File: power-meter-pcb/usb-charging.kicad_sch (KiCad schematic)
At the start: 4 parts, among them J1 USB4105-GF-A, U1 TPD3E001DRLR

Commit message: Assigning footprints, extremely rough idea of size
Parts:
- J1: footprint USB4105-GF-A:GCT_USB4105-GF-A -> USB4105:GCT_USB4105-GF-A
- R1, R4: footprint (none) -> Resistor_SMD:R_0603_1608Metric_Pad0.98x0.95mm_HandSolder
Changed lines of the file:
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@@
 			)
 		)
-		(property "Footprint" ""
+		(property "Footprint" "Resistor_SMD:R_0603_1608Metric_Pad0.98x0.95mm_HandSolder"
 			(at 135.382 74.93 90)
 			(effects
@@
 			)
 		)
-		(property "Footprint" ""
+		(property "Footprint" "Resistor_SMD:R_0603_1608Metric_Pad0.98x0.95mm_HandSolder"
 			(at 61.722 72.39 90)
 			(effects
@@
 			)
 		)
-		(property "Footprint" "USB4105-GF-A:GCT_USB4105-GF-A"
+		(property "Footprint" "USB4105:GCT_USB4105-GF-A"
 			(at 101.6 71.12 0)
 			(effects

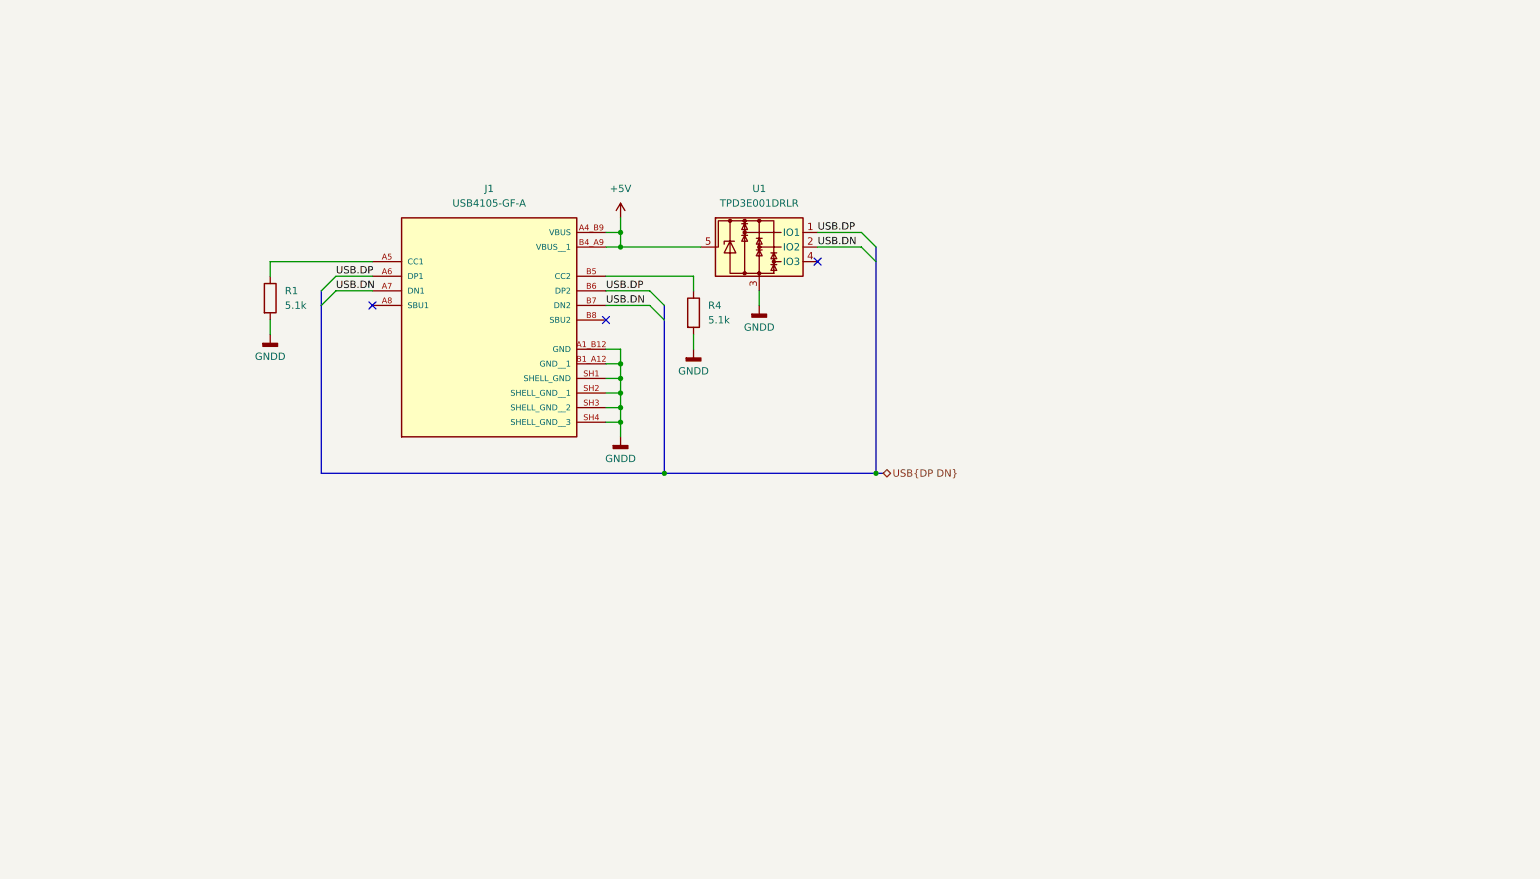
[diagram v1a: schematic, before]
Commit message: Added power supply to PCB
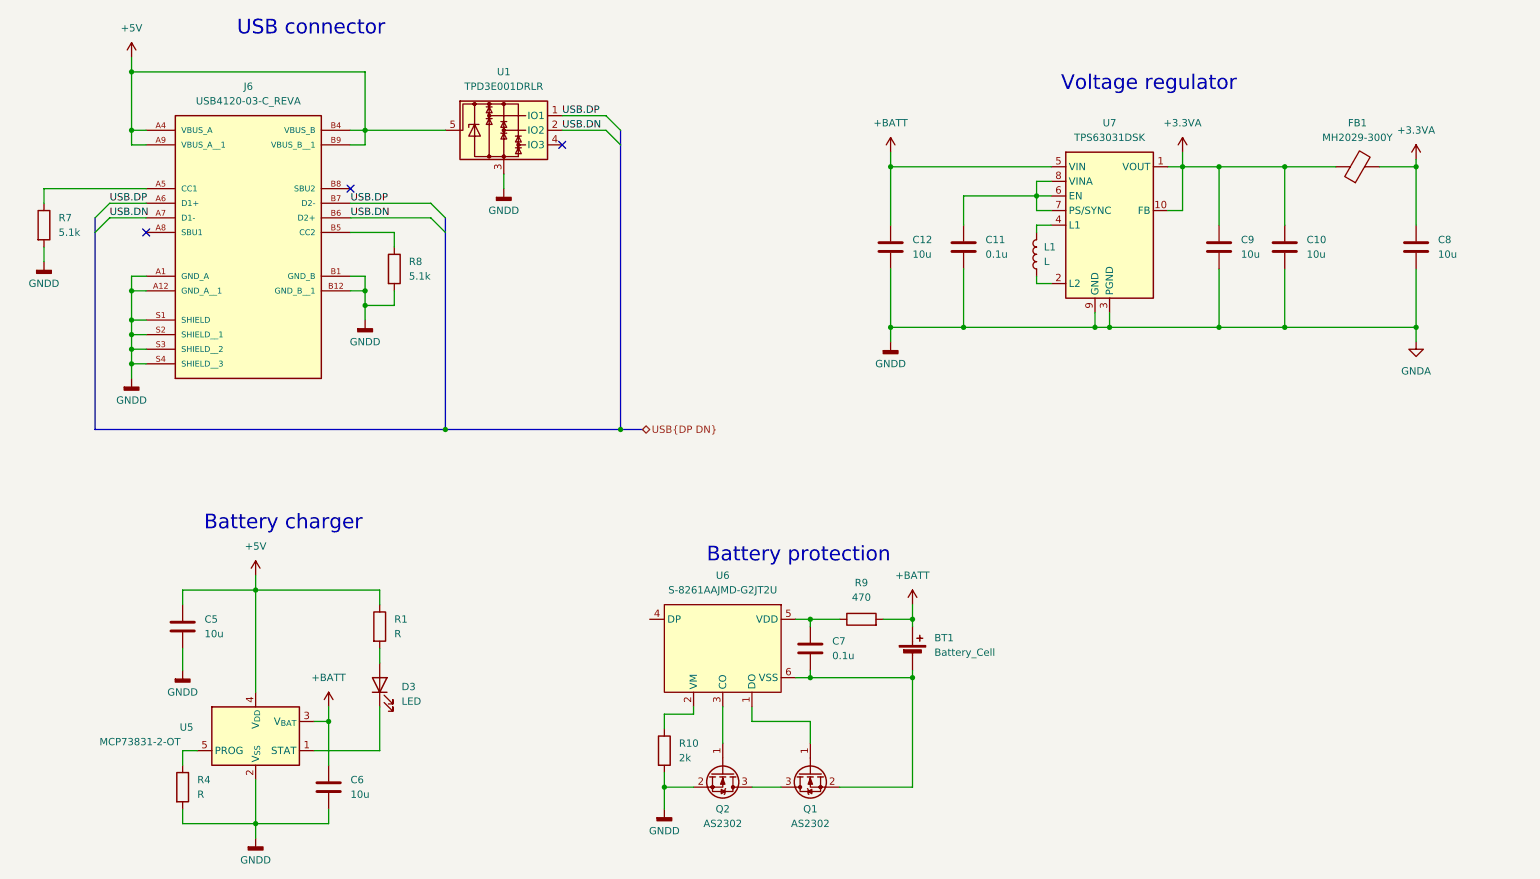
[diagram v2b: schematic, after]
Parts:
- removed J1: USB4105-GF-A, USB4105:GCT_USB4105-GF-A, symbol USB4105:USB4105-GF-A
- added BT1: Battery_Cell, symbol Device:Battery_Cell
- added C10, C12, C5, C6, C8, C9: 10u, symbol Device:C
- added C11, C7: 0.1u, symbol Device:C
- added D3: LED, symbol Device:LED
- added FB1: MH2029-300Y, symbol Device:FerriteBead
- added J6: USB4120-03-C_REVA, USB4120:GCT_USB4120-03-C_REVA, symbol USB4120-03-C_REVA:USB4120-03-C_REVA
- added L1: L, symbol Device:L
- added Q1, Q2: AS2302, symbol Device:Q_NMOS_GSD
- added R10: 2k, symbol Device:R
- added R7, R8: 5.1k, Resistor_SMD:R_0603_1608Metric_Pad0.98x0.95mm_HandSolder, symbol Device:R
- added R9: 470, symbol Device:R
- added U5: MCP73831-2-OT, Package_TO_SOT_SMD:SOT-23-5, symbol Battery_Management:MCP73831-2-OT
- added U6: S-8261AAJMD-G2JT2U, Package_TO_SOT_SMD:SOT-23-6, symbol Custom:S-8261_Battery_protection_IC
- added U7: TPS63031DSK, Package_SON:WSON-10-1EP_2.5x2.5mm_P0.5mm_EP1.2x2mm, symbol Regulator_Switching:TPS63031DSK
- R1, R4: value 5.1k -> R; footprint Resistor_SMD:R_0603_1608Metric_Pad0.98x0.95mm_HandSolder -> (none)
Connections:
- net +5V: now also R1.1, C5.1, J6.A4 (VBUS_A), J6.A9 (VBUS_A__1), J6.B4 (VBUS_B), J6.B9 (VBUS_B__1), U5.4 (V_{DD})
- net USB.DN: now also J6.A7 (D1-), J6.B6 (D2+)
- net USB.DP: now also J6.A6 (D1+), J6.B7 (D2-)
- net at R4.1: now also U5.5 (PROG)
- net GNDD renamed GNDA
- net GNDA: now also C10.2, C11.2, C12.2, C5.2, C6.2, C8.2, C9.2, J6.A1 (GND_A), J6.A12 (GND_A__1), J6.B1 (GND_B), J6.B12 (GND_B__1), J6.S1 (SHIELD), J6.S2 (SHIELD__1), J6.S3 (SHIELD__2), J6.S4 (SHIELD__3), Q2.2 (S), R10.2, R7.2, R8.2, U5.2 (V_{SS}), U7.11 (PGND), U7.3 (PGND), U7.9 (GND); no longer R1.2
- new net: J6.B5 (CC2), R8.1
- new net: D3.2 (A), R1.2
- new net: J6.A5 (CC1), R7.1
- new net: R10.1, U6.2 (VM)
- new net: L1.1, U7.2 (L2)
- new net: L1.2, U7.4 (L1)
- new net: C11.1, U7.6 (EN), U7.7 (PS/SYNC), U7.8 (VINA)
- new net: D3.1 (K), U5.1 (STAT)
- new net: C7.1, R9.1, U6.5 (VDD)
- new net: Q1.1 (G), U6.1 (DO)
- new net: BT1.2 (-), C7.2, Q1.2 (S), U6.6 (VSS)
- new net: Q1.3 (D), Q2.3 (D)
- new net: Q2.1 (G), U6.3 (CO)
- new net +3.3VA: C10.1, C8.1, C9.1, FB1.1, FB1.2, U7.1 (VOUT), U7.10 (FB)
- new net +BATT: BT1.1 (+), C12.1, C6.1, R9.2, U5.3 (V_{BAT}), U7.5 (VIN)
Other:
- note added: "Battery charger"
- note added: "Battery protection"
- note added: "USB connector"
- note added: "Voltage regulator"
- moved on the sheet: U1

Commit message: Started PCB layout
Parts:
- added C15: 0.1u, Capacitor_SMD:C_0603_1608Metric_Pad1.08x0.95mm_HandSolder, symbol Device:C
- added R11, R12: 1M, Resistor_SMD:R_0603_1608Metric_Pad0.98x0.95mm_HandSolder, symbol Device:R
- BT1: footprint (none) -> Connector_JST:JST_EH_B2B-EH-A_1x02_P2.50mm_Vertical
- C10: renamed from C8; footprint (none) -> Capacitor_SMD:C_0603_1608Metric_Pad1.08x0.95mm_HandSolder
- C3: renamed from C5; footprint (none) -> Capacitor_SMD:C_0603_1608Metric_Pad1.08x0.95mm_HandSolder
- C4: renamed from C6; footprint (none) -> Capacitor_SMD:C_0603_1608Metric_Pad1.08x0.95mm_HandSolder
- C5: renamed from C7; footprint (none) -> Capacitor_SMD:C_0603_1608Metric_Pad1.08x0.95mm_HandSolder
- C6: renamed from C12; footprint (none) -> Capacitor_SMD:C_0603_1608Metric_Pad1.08x0.95mm_HandSolder
- C7: renamed from C11; footprint (none) -> Capacitor_SMD:C_0603_1608Metric_Pad1.08x0.95mm_HandSolder
- C8: renamed from C9; footprint (none) -> Capacitor_SMD:C_0603_1608Metric_Pad1.08x0.95mm_HandSolder
- C9: renamed from C10; footprint (none) -> Capacitor_SMD:C_0603_1608Metric_Pad1.08x0.95mm_HandSolder
- D3: footprint (none) -> LED_SMD:LED_0603_1608Metric_Pad1.05x0.95mm_HandSolder
- FB1: footprint (none) -> Inductor_SMD:L_0805_2012Metric
- L1: value L -> 4.7uH; footprint (none) -> Inductor_SMD:L_Murata_DFE201610P
- Q1: renamed from Q2; footprint (none) -> Package_TO_SOT_SMD:TSOT-23
- Q2: renamed from Q1; footprint (none) -> Package_TO_SOT_SMD:TSOT-23
- R10: renamed from R9; footprint (none) -> Resistor_SMD:R_0603_1608Metric_Pad0.98x0.95mm_HandSolder
- R6: renamed from R4; value R -> 2.2k; footprint (none) -> Resistor_SMD:R_0603_1608Metric_Pad0.98x0.95mm_HandSolder
- R7: renamed from R1; value R -> 470; footprint (none) -> Resistor_SMD:R_0603_1608Metric_Pad0.98x0.95mm_HandSolder
- R9: renamed from R10; footprint (none) -> Resistor_SMD:R_0603_1608Metric_Pad0.98x0.95mm_HandSolder
- renumbered J6 to J3, R7 to R5, U5 to U3, U1 to U4, U6 to U5, U7 to U6
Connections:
- net +3.3VA: no longer C8.1, C9.1, FB1.1, U6.1 (VOUT), U6.10 (FB)
- net +BATT: now also R12.1
- net GNDA: no longer C3.2, C4.2, C6.2, C7.2, C8.2, C9.2, J3.A1 (GND_A), J3.A12 (GND_A__1), J3.B1 (GND_B), J3.B12 (GND_B__1), J3.S1 (SHIELD), J3.S2 (SHIELD__1), J3.S3 (SHIELD__2), J3.S4 (SHIELD__3), Q1.2 (S), R5.2, R6.2, R8.2, R9.2, U3.2 (V_{SS}), U4.3, U6.11 (PGND), U6.3 (PGND), U6.9 (GND)
- net at C7.1, U6.6 (EN), U6.8 (VINA): no longer U6.7 (PS/SYNC)
- new net +3.3V: C8.1, C9.1, FB1.1, U6.1 (VOUT), U6.10 (FB)
- new net Battery voltage: C15.1, R11.1, R12.2
- new net GNDD: C15.2, C3.2, C4.2, C6.2, C7.2, C8.2, C9.2, J3.A1 (GND_A), J3.A12 (GND_A__1), J3.B1 (GND_B), J3.B12 (GND_B__1), J3.S1 (SHIELD), J3.S2 (SHIELD__1), J3.S3 (SHIELD__2), J3.S4 (SHIELD__3), Q1.2 (S), R11.2, R5.2, R6.2, R8.2, R9.2, U3.2 (V_{SS}), U4.3, U6.11 (PGND), U6.3 (PGND), U6.9 (GND)
- new net Power save: U6.7 (PS/SYNC)
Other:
- note added: "Battery voltage measurement"
- moved on the sheet: BT1, C6, C7, FB1, L1

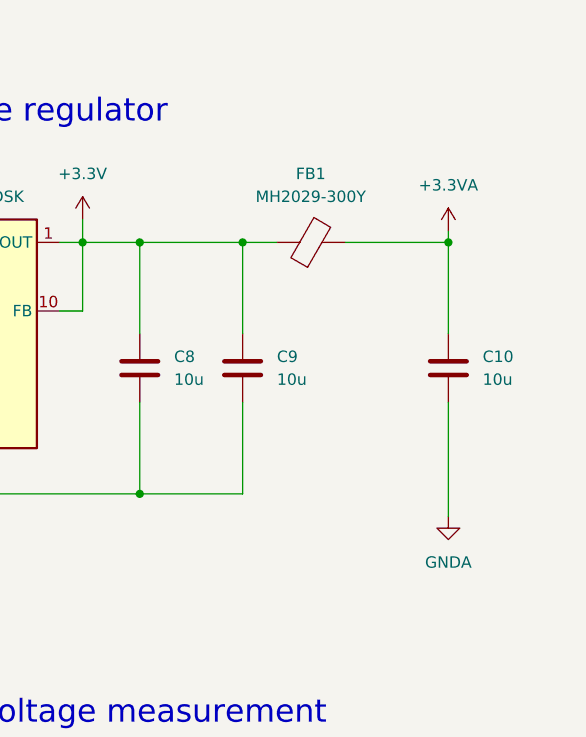
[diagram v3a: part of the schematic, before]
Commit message: Adding filtering and pullup resistors, board layout
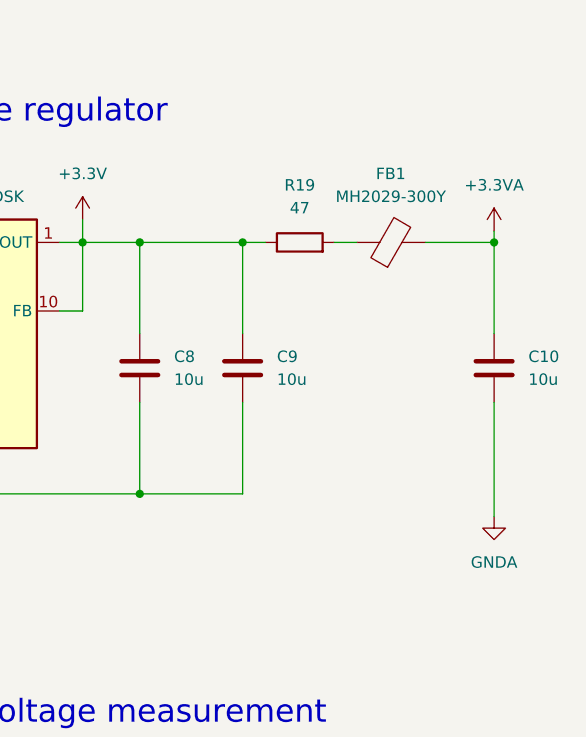
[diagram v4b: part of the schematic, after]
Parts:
- added R19: 47, Resistor_SMD:R_0603_1608Metric_Pad0.98x0.95mm_HandSolder, symbol Device:R
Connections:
- net +3.3V: now also R19.1; no longer FB1.1
- new net: FB1.1, R19.2
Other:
- moved on the sheet: C10, FB1
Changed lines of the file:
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@@
 	)
 	(junction
-		(at 262.89 49.53)
+		(at 267.97 49.53)
 		(diameter 0)
 		(color 0 0 0 0)
@@
 	(wire
 		(pts
-			(xy 262.89 67.31) (xy 262.89 80.01)
+			(xy 267.97 67.31) (xy 267.97 80.01)
 		)
 		(stroke
@@
 	(wire
 		(pts
-			(xy 251.46 49.53) (xy 262.89 49.53)
-		)
-		(stroke
-			(width 0)
-			(type default)
-		)
-	)
-	(wire
-		(pts
 			(xy 80.01 43.18) (xy 80.01 33.02)
 		)
@@
 	(wire
 		(pts
-			(xy 262.89 48.26) (xy 262.89 49.53)
+			(xy 267.97 48.26) (xy 267.97 49.53)
 		)
 		(stroke
@@
 	(wire
 		(pts
-			(xy 240.03 49.53) (xy 243.84 49.53)
+			(xy 240.03 49.53) (xy 242.57 49.53)
 		)
 		(stroke
@@
 	(wire
 		(pts
+			(xy 260.35 49.53) (xy 267.97 49.53)
+		)
+		(stroke
+			(width 0)
+			(type default)
+		)
+	)
+	(wire
+		(pts
 			(xy 219.71 137.16) (xy 219.71 139.7)
 		)
@@
 	(wire
 		(pts
-			(xy 262.89 49.53) (xy 262.89 59.69)
+			(xy 267.97 49.53) (xy 267.97 59.69)
 		)
 		(stroke
@@
 		(pts
 			(xy 157.48 128.27) (xy 162.56 128.27)
+		)
+		(stroke
+			(width 0)
+			(type default)
+		)
+	)
+	(wire
+		(pts
+			(xy 250.19 49.53) (xy 252.73 49.53)
 		)
 		(stroke
@@
 	(symbol
 		(lib_id "Device:R")
+		(at 246.38 49.53 90)
+		(unit 1)
+		(exclude_from_sim no)
+		(in_bom yes)
+		(on_board yes)
+		(dnp no)
+		(fields_autoplaced yes)
+		(property "Reference" "R19"
+			(at 246.38 43.18 90)
+			(effects
+				(font
+					(size 1.27 1.27)
+				)
+			)
+		)
+		(property "Value" "47"
+			(at 246.38 45.72 90)
+			(effects
+				(font
+					(size 1.27 1.27)
+				)
+			)
+		)
+		(property "Footprint" "Resistor_SMD:R_0603_1608Metric_Pad0.98x0.95mm_HandSolder"
+			(at 246.38 51.308 90)
+			(effects
+				(font
+					(size 1.27 1.27)
+				)
+				(hide yes)
+			)
+		)
+		(property "Datasheet" "~"
+			(at 246.38 49.53 0)
+			(effects
+				(font
+					(size 1.27 1.27)
+				)
+				(hide yes)
+			)
+		)
+		(property "Description" "Resistor"
+			(at 246.38 49.53 0)
+			(effects
+				(font
+					(size 1.27 1.27)
+				)
+				(hide yes)
+			)
+		)
+		(pin "2"
+		)
+		(pin "1"
+		)
+		(instances
+			(project "power-meter-pcb"
+				(path "/73d1dc3f-3725-4767-8c11-2d32e15ee0d6/4fb726d4-a68e-4ad8-a718-58b82440e761"
+					(reference "R19")
+					(unit 1)
+				)
+			)
+		)
+	)
+	(symbol
+		(lib_id "Device:R")
 		(at 219.71 118.11 0)
 		(unit 1)
@@
 	(symbol
 		(lib_id "power:+3.3VA")
-		(at 262.89 48.26 0)
+		(at 267.97 48.26 0)
 		(unit 1)
 		(exclude_from_sim no)
@@
 		(fields_autoplaced yes)
 		(property "Reference" "#PWR030"
-			(at 262.89 52.07 0)
+			(at 267.97 52.07 0)
 			(effects
 				(font
@@
 		)
 		(property "Value" "+3.3VA"
-			(at 262.89 43.18 0)
+			(at 267.97 43.18 0)
 			(effects
 				(font
@@
 		)
 		(property "Footprint" ""
-			(at 262.89 48.26 0)
+			(at 267.97 48.26 0)
 			(effects
 				(font
@@
 		)
 		(property "Datasheet" ""
-			(at 262.89 48.26 0)
+			(at 267.97 48.26 0)
 			(effects
 				(font
@@
 		)
 		(property "Description" "Power symbol creates a global label with name \"+3.3VA\""
-			(at 262.89 48.26 0)
+			(at 267.97 48.26 0)
 			(effects
 				(font
@@
 	(symbol
 		(lib_id "Device:FerriteBead")
-		(at 247.65 49.53 90)
+		(at 256.54 49.53 90)
 		(unit 1)
 		(exclude_from_sim no)
@@
 		(fields_autoplaced yes)
 		(property "Reference" "FB1"
-			(at 247.5992 41.91 90)
+			(at 256.4892 41.91 90)
 			(effects
 				(font
@@
 		)
 		(property "Value" "MH2029-300Y"
-			(at 247.5992 44.45 90)
+			(at 256.4892 44.45 90)
 			(effects
 				(font
@@
 		)
 		(property "Footprint" "Inductor_SMD:L_0805_2012Metric"
-			(at 247.65 51.308 90)
+			(at 256.54 51.308 90)
 			(effects
 				(font
@@
 		)
 		(property "Datasheet" "~"
-			(at 247.65 49.53 0)
+			(at 256.54 49.53 0)
 			(effects
 				(font
@@
 		)
 		(property "Description" "Ferrite bead"
-			(at 247.65 49.53 0)
+			(at 256.54 49.53 0)
 			(effects
 				(font
@@
 	(symbol
 		(lib_id "Device:C")
-		(at 262.89 63.5 0)
+		(at 267.97 63.5 0)
 		(unit 1)
 		(exclude_from_sim no)
@@
 		(fields_autoplaced yes)
 		(property "Reference" "C10"
-			(at 266.7 62.2299 0)
+			(at 271.78 62.2299 0)
 			(effects
 				(font
@@
 		)
 		(property "Value" "10u"
-			(at 266.7 64.7699 0)
+			(at 271.78 64.7699 0)
 			(effects
 				(font
@@
 		)
 		(property "Footprint" "Capacitor_SMD:C_0603_1608Metric_Pad1.08x0.95mm_HandSolder"
-			(at 263.8552 67.31 0)
+			(at 268.9352 67.31 0)
 			(effects
 				(font
@@
 		)
 		(property "Datasheet" "~"
-			(at 262.89 63.5 0)
+			(at 267.97 63.5 0)
 			(effects
 				(font
@@
 		)
 		(property "Description" "Unpolarized capacitor"
-			(at 262.89 63.5 0)
+			(at 267.97 63.5 0)
 			(effects
 				(font
@@
 	(symbol
 		(lib_id "power:GNDA")
-		(at 262.89 80.01 0)
+		(at 267.97 80.01 0)
 		(unit 1)
 		(exclude_from_sim no)
@@
 		(fields_autoplaced yes)
 		(property "Reference" "#PWR031"
-			(at 262.89 86.36 0)
+			(at 267.97 86.36 0)
 			(effects
 				(font
@@
 		)
 		(property "Value" "GNDA"
-			(at 262.89 85.09 0)
+			(at 267.97 85.09 0)
 			(effects
 				(font
@@
 		)
 		(property "Footprint" ""
-			(at 262.89 80.01 0)
+			(at 267.97 80.01 0)
 			(effects
 				(font
@@
 		)
 		(property "Datasheet" ""
-			(at 262.89 80.01 0)
+			(at 267.97 80.01 0)
 			(effects
 				(font
@@
 		)
 		(property "Description" "Power symbol creates a global label with name \"GNDA\" , analog ground"
-			(at 262.89 80.01 0)
-			(effects
-				(font
+			(at 267.97 80.01 0)
+			(effects
+				(font
